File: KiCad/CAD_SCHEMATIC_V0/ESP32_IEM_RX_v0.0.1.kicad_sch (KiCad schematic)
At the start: 0 parts

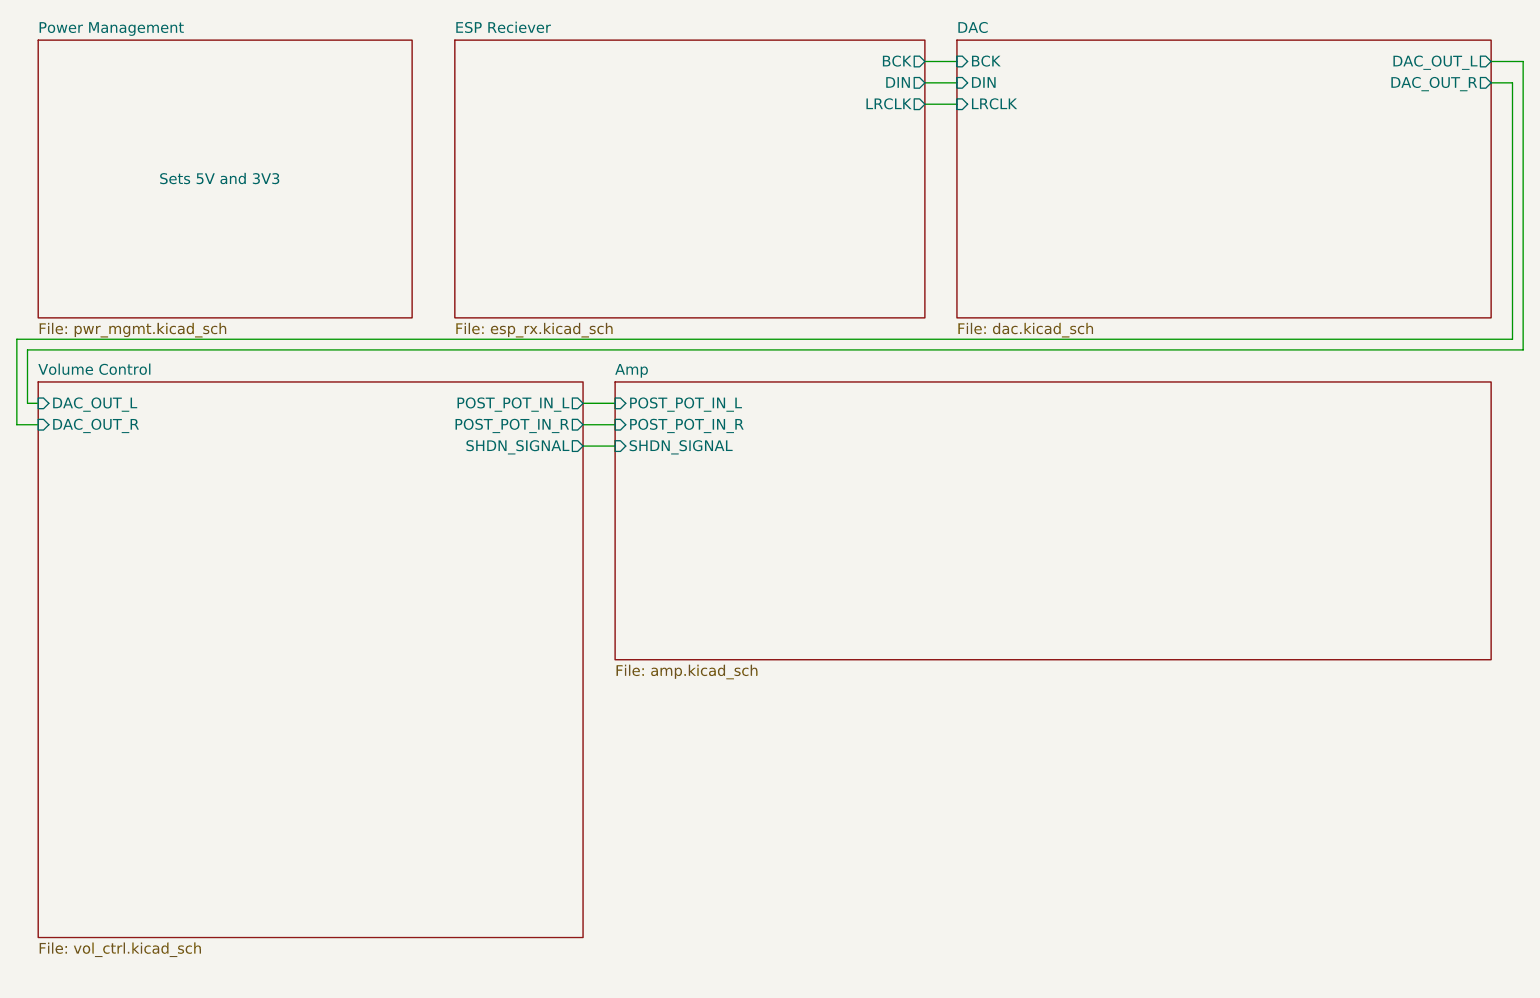
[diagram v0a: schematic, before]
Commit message: Resolved ERC errors.
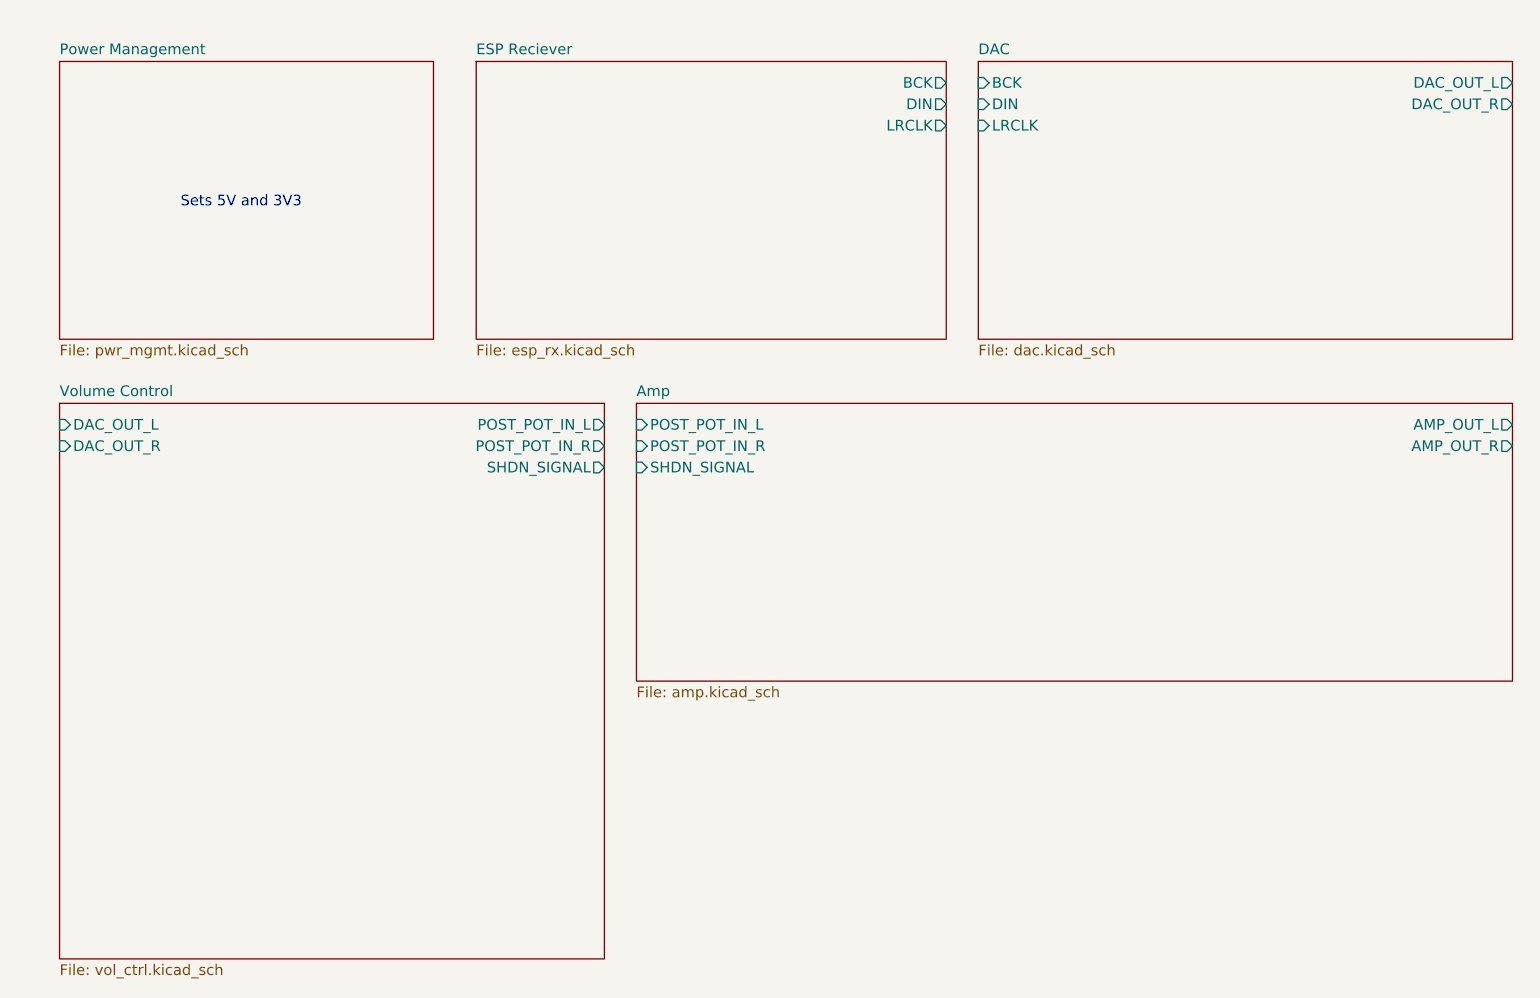
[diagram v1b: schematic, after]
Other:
- sheet Amp ports: added AMP_OUT_L, AMP_OUT_R; removed none
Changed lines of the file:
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@@
 		(title "ESP32 Wireless IEM Rig Reciever")
 		(date "2026-08-04")
-		(rev "0.0.3")
+		(rev "0.0.1")
 		(company "damian m")
 		(comment 1 "Data: ESP -> DAC -> AMP-> 3.5mm Jack.")
@@
 	(text "Sets 5V and 3V3"
 		(exclude_from_sim no)
-		(at 39.37 38.354 0)
+		(at 41.91 40.894 0)
 		(effects
 			(font
@@
 		)
 	)
-	(wire
-		(pts
-			(xy 193.04 26.67) (xy 193.04 57.15)
-		)
-		(stroke
-			(width 0)
-			(type default)
-		)
-	)
-	(wire
-		(pts
-			(xy 194.31 58.42) (xy 16.51 58.42)
-		)
-		(stroke
-			(width 0)
-			(type default)
-		)
-	)
-	(wire
-		(pts
-			(xy 82.55 69.85) (xy 86.36 69.85)
-		)
-		(stroke
-			(width 0)
-			(type default)
-		)
-	)
-	(wire
-		(pts
-			(xy 82.55 67.31) (xy 86.36 67.31)
-		)
-		(stroke
-			(width 0)
-			(type default)
-		)
-	)
-	(wire
-		(pts
-			(xy 190.5 26.67) (xy 193.04 26.67)
-		)
-		(stroke
-			(width 0)
-			(type default)
-		)
-	)
-	(wire
-		(pts
-			(xy 193.04 57.15) (xy 15.24 57.15)
-		)
-		(stroke
-			(width 0)
-			(type default)
-		)
-	)
-	(wire
-		(pts
-			(xy 15.24 67.31) (xy 17.78 67.31)
-		)
-		(stroke
-			(width 0)
-			(type default)
-		)
-	)
-	(wire
-		(pts
-			(xy 15.24 57.15) (xy 15.24 67.31)
-		)
-		(stroke
-			(width 0)
-			(type default)
-		)
-	)
-	(wire
-		(pts
-			(xy 82.55 64.77) (xy 86.36 64.77)
-		)
-		(stroke
-			(width 0)
-			(type default)
-		)
-	)
-	(wire
-		(pts
-			(xy 194.31 24.13) (xy 194.31 58.42)
-		)
-		(stroke
-			(width 0)
-			(type default)
-		)
-	)
-	(wire
-		(pts
-			(xy 190.5 24.13) (xy 194.31 24.13)
-		)
-		(stroke
-			(width 0)
-			(type default)
-		)
-	)
-	(wire
-		(pts
-			(xy 123.19 26.67) (xy 127 26.67)
-		)
-		(stroke
-			(width 0)
-			(type default)
-		)
-	)
-	(wire
-		(pts
-			(xy 16.51 58.42) (xy 16.51 64.77)
-		)
-		(stroke
-			(width 0)
-			(type default)
-		)
-	)
-	(wire
-		(pts
-			(xy 123.19 24.13) (xy 127 24.13)
-		)
-		(stroke
-			(width 0)
-			(type default)
-		)
-	)
-	(wire
-		(pts
-			(xy 123.19 29.21) (xy 127 29.21)
-		)
-		(stroke
-			(width 0)
-			(type default)
-		)
-	)
-	(wire
-		(pts
-			(xy 16.51 64.77) (xy 17.78 64.77)
-		)
-		(stroke
-			(width 0)
-			(type default)
-		)
-	)
-	(sheet
-		(at 67.31 21.59)
+	(sheet
+		(at 69.85 24.13)
 		(size 55.88 33.02)
 		(exclude_from_sim no)
@@
 		)
 		(property "Sheetname" "ESP Reciever"
-			(at 67.31 20.8784 0)
+			(at 69.85 23.4184 0)
 			(show_name yes)
 			(do_not_autoplace no)
@@
 		)
 		(property "Sheetfile" "esp_rx.kicad_sch"
-			(at 67.31 55.1946 0)
+			(at 69.85 57.7346 0)
 			(show_name no)
 			(do_not_autoplace no)
@@
 		)
 		(pin "BCK" output
-			(at 123.19 24.13 0)
+			(at 125.73 26.67 0)
 			(effects
 				(font
@@
 		)
 		(pin "DIN" output
-			(at 123.19 26.67 0)
+			(at 125.73 29.21 0)
 			(effects
 				(font
@@
 		)
 		(pin "LRCLK" output
-			(at 123.19 29.21 0)
+			(at 125.73 31.75 0)
 			(effects
 				(font
@@
 	)
 	(sheet
-		(at 127 21.59)
+		(at 129.54 24.13)
 		(size 63.5 33.02)
 		(exclude_from_sim no)
@@
 		)
 		(property "Sheetname" "DAC"
-			(at 127 20.8784 0)
+			(at 129.54 23.4184 0)
 			(show_name yes)
 			(do_not_autoplace no)
@@
 		)
 		(property "Sheetfile" "dac.kicad_sch"
-			(at 127 55.1946 0)
+			(at 129.54 57.7346 0)
 			(show_name no)
 			(do_not_autoplace no)
@@
 		)
 		(pin "BCK" input
-			(at 127 24.13 180)
+			(at 129.54 26.67 180)
 			(effects
 				(font
@@
 		)
 		(pin "DIN" input
-			(at 127 26.67 180)
+			(at 129.54 29.21 180)
 			(effects
 				(font
@@
 		)
 		(pin "LRCLK" input
-			(at 127 29.21 180)
+			(at 129.54 31.75 180)
 			(effects
 				(font
@@
 		)
 		(pin "DAC_OUT_L" output
-			(at 190.5 24.13 0)
+			(at 193.04 26.67 0)
 			(effects
 				(font
@@
 		)
 		(pin "DAC_OUT_R" output
-			(at 190.5 26.67 0)
+			(at 193.04 29.21 0)
 			(effects
 				(font
@@
 	)
 	(sheet
-		(at 17.78 21.59)
+		(at 20.32 24.13)
 		(size 44.45 33.02)
 		(exclude_from_sim no)
@@
 		)
 		(property "Sheetname" "Power Management"
-			(at 17.78 20.8784 0)
+			(at 20.32 23.4184 0)
 			(show_name yes)
 			(do_not_autoplace no)
@@
 		)
 		(property "Sheetfile" "pwr_mgmt.kicad_sch"
-			(at 17.78 55.1946 0)
+			(at 20.32 57.7346 0)
 			(show_name yes)
 			(do_not_autoplace no)
@@
 	)
 	(sheet
-		(at 86.36 62.23)
+		(at 88.9 64.77)
 		(size 104.14 33.02)
 		(exclude_from_sim no)
@@
 		)
 		(property "Sheetname" "Amp"
-			(at 86.36 61.5184 0)
+			(at 88.9 64.0584 0)
 			(show_name yes)
 			(do_not_autoplace no)
@@
 		)
 		(property "Sheetfile" "amp.kicad_sch"
-			(at 86.36 95.8346 0)
+			(at 88.9 98.3746 0)
 			(show_name no)
 			(do_not_autoplace no)
@@
 		)
 		(pin "POST_POT_IN_L" input
-			(at 86.36 64.77 180)
+			(at 88.9 67.31 180)
 			(effects
 				(font
@@
 		)
 		(pin "POST_POT_IN_R" input
-			(at 86.36 67.31 180)
+			(at 88.9 69.85 180)
 			(effects
 				(font
@@
 		)
 		(pin "SHDN_SIGNAL" input
-			(at 86.36 69.85 180)
-			(effects
-				(font
-					(size 1.27 1.27)
-				)
-				(justify left)
+			(at 88.9 72.39 180)
+			(effects
+				(font
+					(size 1.27 1.27)
+				)
+				(justify left)
+			)
+		)
+		(pin "AMP_OUT_L" output
+			(at 193.04 67.31 0)
+			(effects
+				(font
+					(size 1.27 1.27)
+				)
+				(justify right)
+			)
+		)
+		(pin "AMP_OUT_R" output
+			(at 193.04 69.85 0)
+			(effects
+				(font
+					(size 1.27 1.27)
+				)
+				(justify right)
 			)
 		)
@@
 	)
 	(sheet
-		(at 17.78 62.23)
+		(at 20.32 64.77)
 		(size 64.77 66.04)
 		(exclude_from_sim no)
@@
 		)
 		(property "Sheetname" "Volume Control"
-			(at 17.78 61.5184 0)
+			(at 20.32 64.0584 0)
 			(show_name yes)
 			(do_not_autoplace no)
@@
 		)
 		(property "Sheetfile" "vol_ctrl.kicad_sch"
-			(at 17.78 128.8546 0)
+			(at 20.32 131.3946 0)
 			(show_name no)
 			(do_not_autoplace no)
@@
 		)
 		(pin "DAC_OUT_L" input
-			(at 17.78 64.77 180)
+			(at 20.32 67.31 180)
 			(effects
 				(font
@@
 		)
 		(pin "DAC_OUT_R" input
-			(at 17.78 67.31 180)
+			(at 20.32 69.85 180)
 			(effects
 				(font
@@
 		)
 		(pin "POST_POT_IN_L" output
-			(at 82.55 64.77 0)
+			(at 85.09 67.31 0)
 			(effects
 				(font
@@
 		)
 		(pin "POST_POT_IN_R" output
-			(at 82.55 67.31 0)
+			(at 85.09 69.85 0)
 			(effects
 				(font
@@
 		)
 		(pin "SHDN_SIGNAL" output
-			(at 82.55 69.85 0)
-			(effects
-				(font
+			(at 85.09 72.39 0)
+			(effects
+				(font
